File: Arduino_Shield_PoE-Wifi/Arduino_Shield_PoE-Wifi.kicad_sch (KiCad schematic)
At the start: 11 parts, among them J1 Conn_02x08, J2 Conn_02x08, J3 PINHD_1x2_Female, J4 PINHD_1x2_Female, SW1 Push_Button

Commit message: Update
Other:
- sheet Power ports: added +3V3A, +3V3B, +3V3C, GNDA, GNDB, GNDC; removed +3V3_1, +3V3_2, GND_3V3_1, GND_3V3_2, PB7
- sheet PowerOverEthernet ports: added +3V3B, EARTH, GNDA, GNDB, GNDPWR; removed +3V3D
- sheet Wifi ports: added +3V3C, +5V, CFG_3V3, CFG_5V, CS_3V3, CS_5V, EN_3V3, EN_5V, GND, GNDC, IRQ, MISO_3V3, MISO_5V, MOSI_3V3, MOSI_5V, RST_3V3, RST_5V, SCK_3V3, SCK_5V, WAKE_3V3, WAKE_5V; removed none
- moved on the sheet: ADC1, ADC2, COM1, J1, J2, J3, J4, PWM1, PWM2, PWR1, SW1

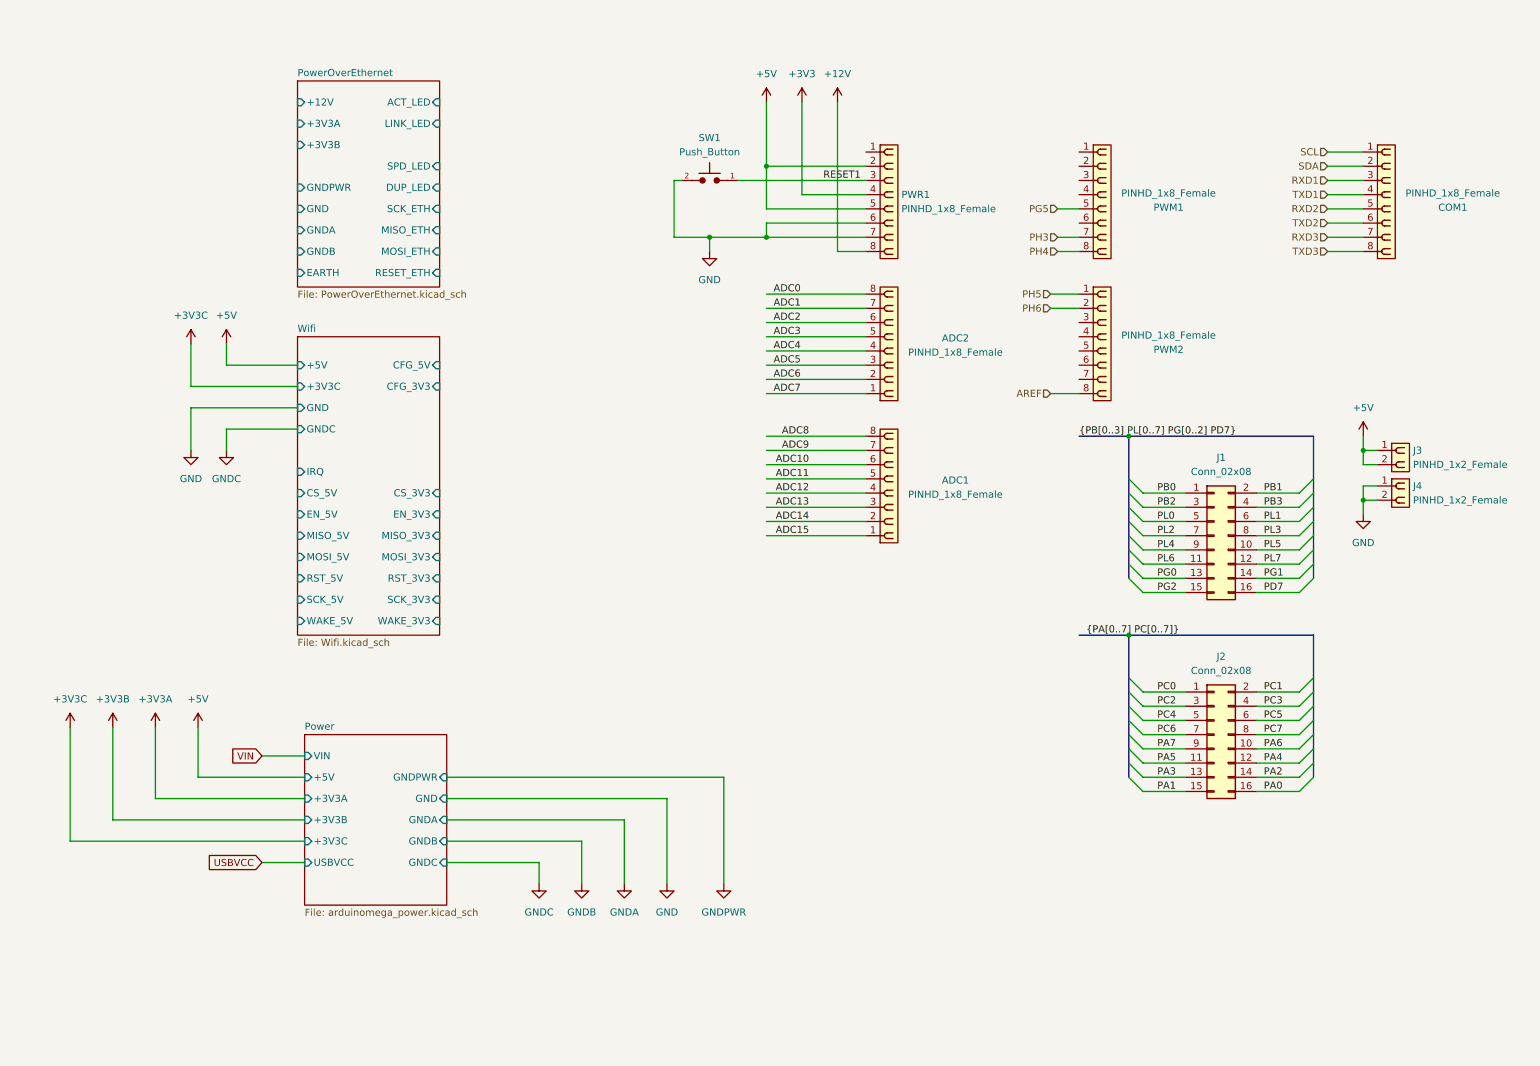
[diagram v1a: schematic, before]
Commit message: Change the wifi module
Replace ATWINC with ESP8266
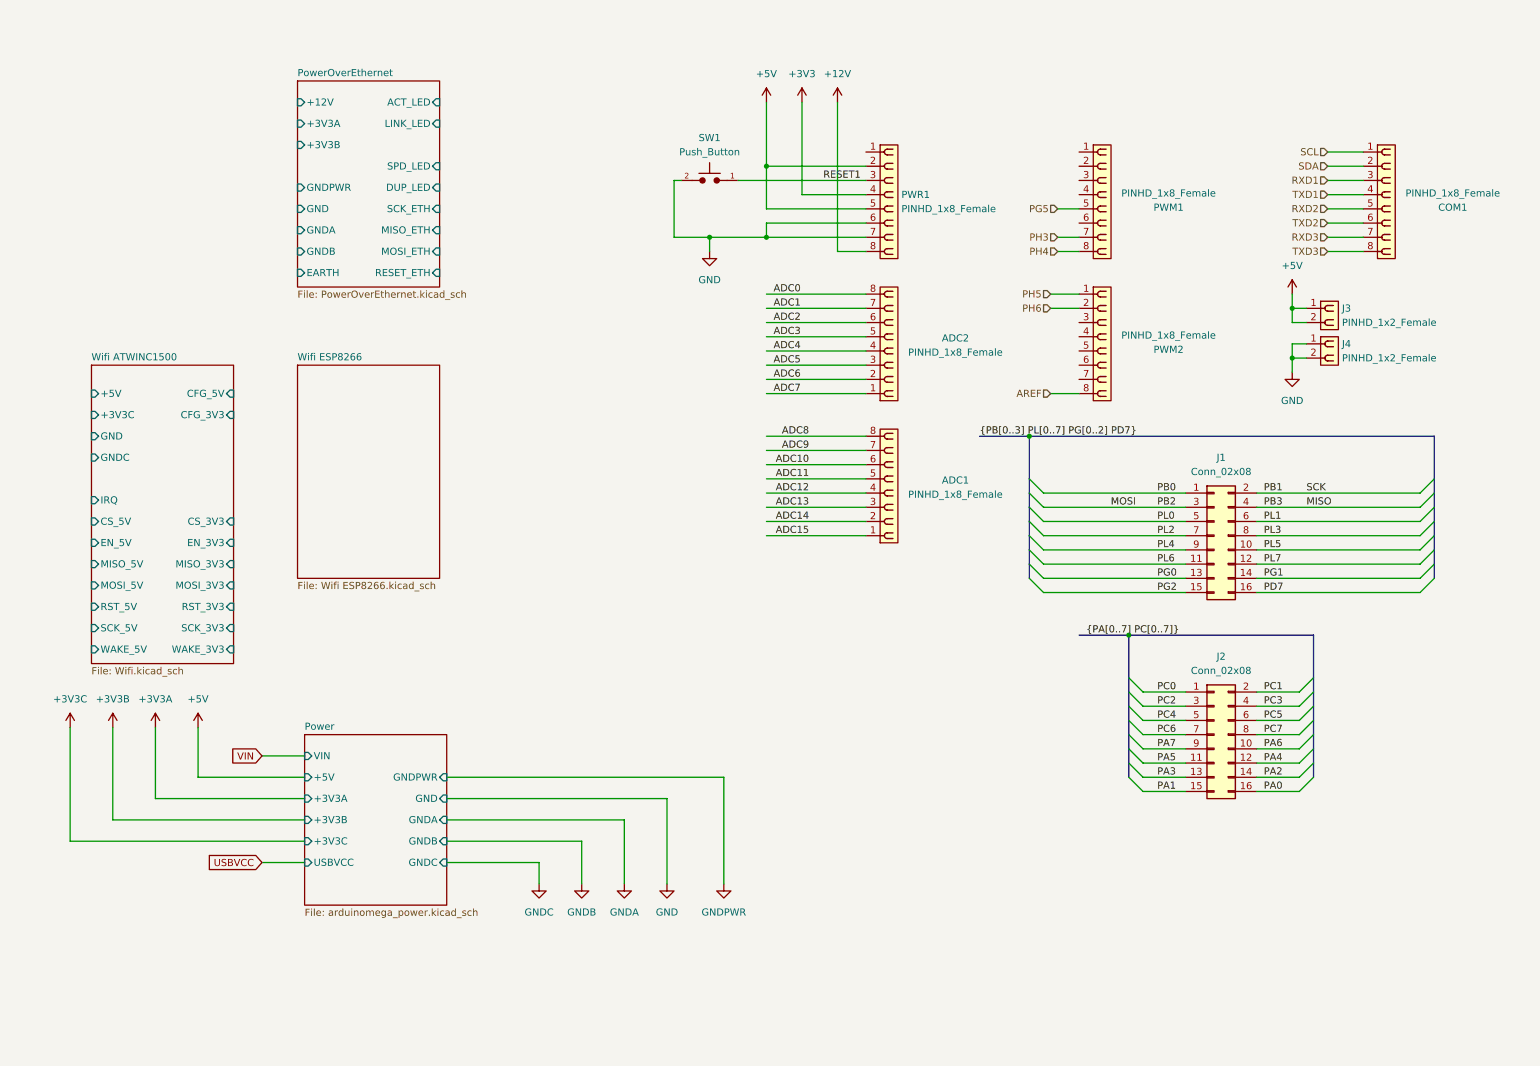
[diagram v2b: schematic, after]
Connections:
- net PB2 renamed MOSI
- net PB3 renamed MISO
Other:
- sheet Wifi renamed Wifi ATWINC1500
- added sheet Wifi ESP8266 (Wifi ESP8266.kicad_sch)
- moved on the sheet: J3, J4

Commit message: fixing schematics
Fix using ESP8266 12-E
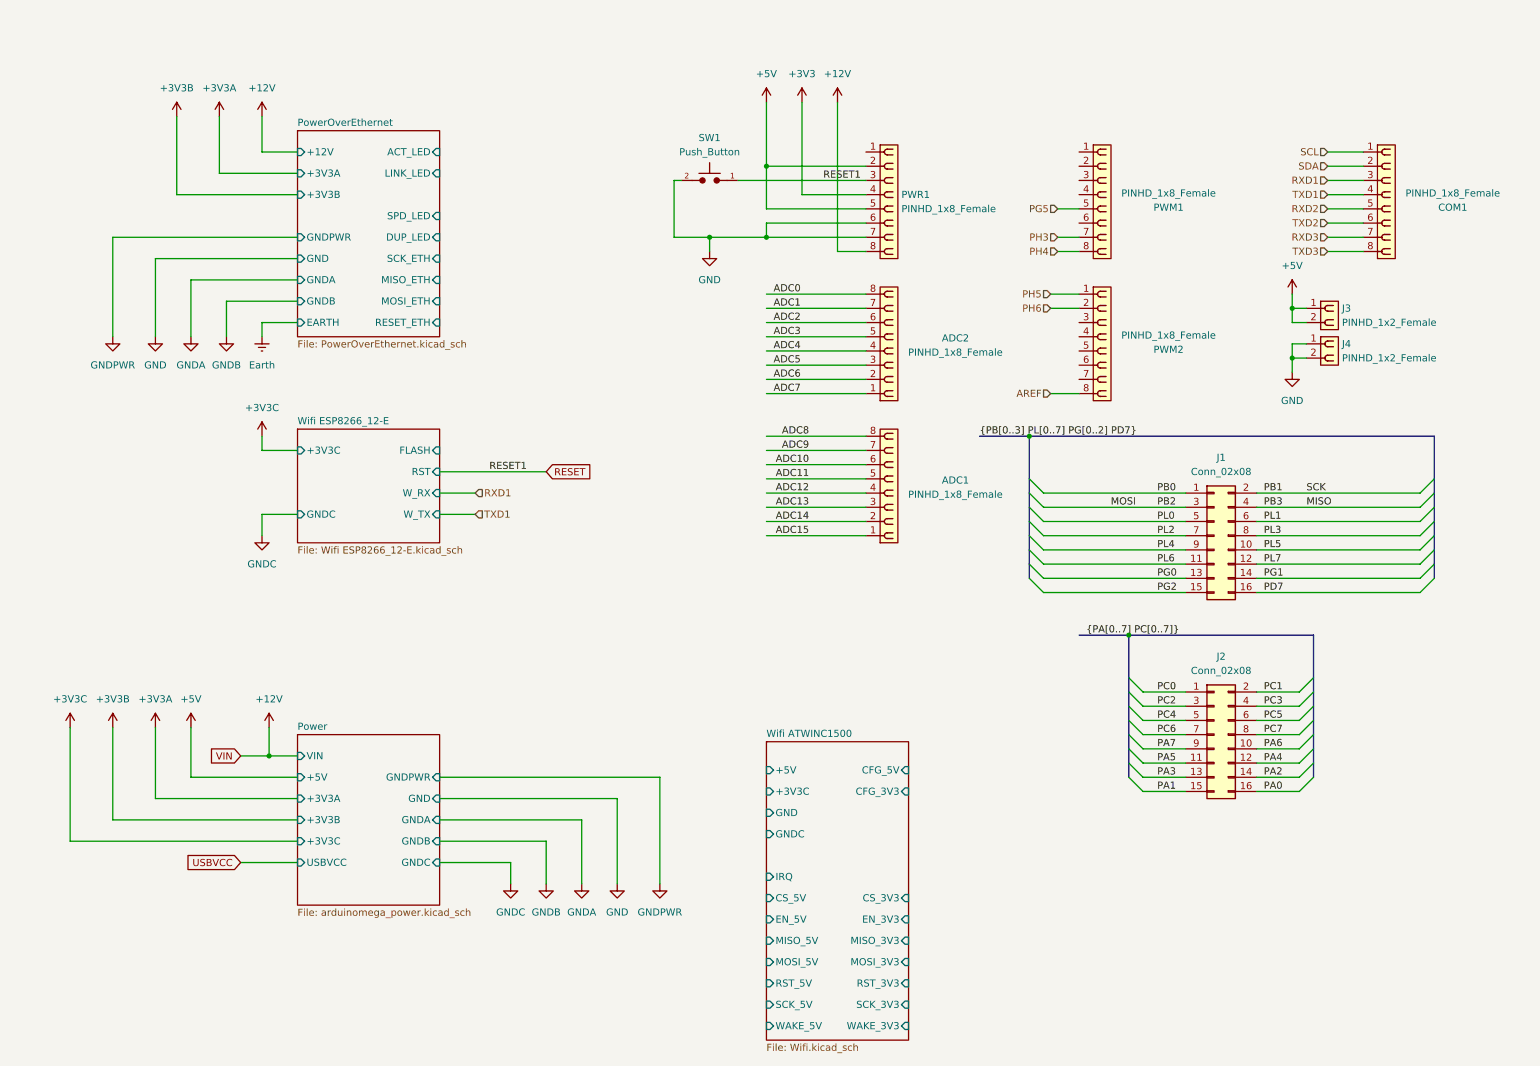
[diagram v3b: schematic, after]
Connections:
- net RESET1 renamed RESET
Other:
- sheet Wifi ESP8266 renamed Wifi ESP8266_12-E
- sheet Wifi ESP8266_12-E: file Wifi ESP8266.kicad_sch -> Wifi ESP8266_12-E.kicad_sch
- sheet Wifi ESP8266_12-E ports: added +3V3C, FLASH, GNDC, RST, W_RX, W_TX; removed none

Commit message: Update fix schematics
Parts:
- added ICSP1: ICSP_Connector_Female, Connector_PinSocket_2.54mm:PinSocket_2x03_P2.54mm_Vertical, symbol PCM_SL_Connectors:ICSP_Connector
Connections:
- net +5V: now also ICSP1.2 (VCC)
- net GND: now also ICSP1.6 (GND)
- net MISO: now also ICSP1.1 (MISO)
- net MOSI: now also ICSP1.4 (MOSI)
- net AREF: no longer names the net of PWM2.8
- net PB1 renamed SCK
- net SCK: now also ICSP1.3 (SCK)
- net PG5: no longer names the net of PWM1.5
- net PH3: no longer names the net of PWM1.7
- net PH4: no longer names the net of PWM1.8
- net PH5: no longer names the net of PWM2.1
- net PH6: no longer names the net of PWM2.2
- net RESET renamed RESET1
- net RESET1: now also ICSP1.5 (~{RST)
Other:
- sheet PowerOverEthernet ports: added none; removed ACT_LED, DUP_LED, LINK_LED, SPD_LED
- moved on the sheet: ADC1, ADC2
